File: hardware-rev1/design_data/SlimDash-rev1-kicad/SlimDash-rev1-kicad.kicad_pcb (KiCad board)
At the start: 2 copper layers, 157.1 x 131.5 mm, 140 parts, among them J1 AudioJack4, J2 AudioJack4, U1 TLV73333PDBV, U2 RP2040, U3 W25Q128JVS, Y1 Crystal_GND24

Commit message: update submodule
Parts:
- USB1: footprint ai03-2725_Type-C:HRO-TYPE-C-31-M-12-Assembly -> mzm_LCSC:USB-C_SMD-TYPE-C-31-M-12
- moved USB1 5.05 mm to (180.8, 43.5)
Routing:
- net Net-(LED31-DIN): track 0.00 -> 43.1 mm, vias 0 -> 4
- net Net-(LED33-DIN): track 0.00 -> 34.0 mm, vias 0 -> 5
- net Net-(LED34-DIN): track 0.00 -> 29.5 mm, vias 0 -> 2
- net Net-(LED32-DIN): track 4.70 -> 34.0 mm, vias 1 -> 3
- net Net-(LED30-DIN): track 0.00 -> 26.7 mm, vias 0 -> 2
- net Net-(JP1-B): track 7.71 -> 13.9 mm, vias 0 -> 1
- net GND: vias 89 -> 216

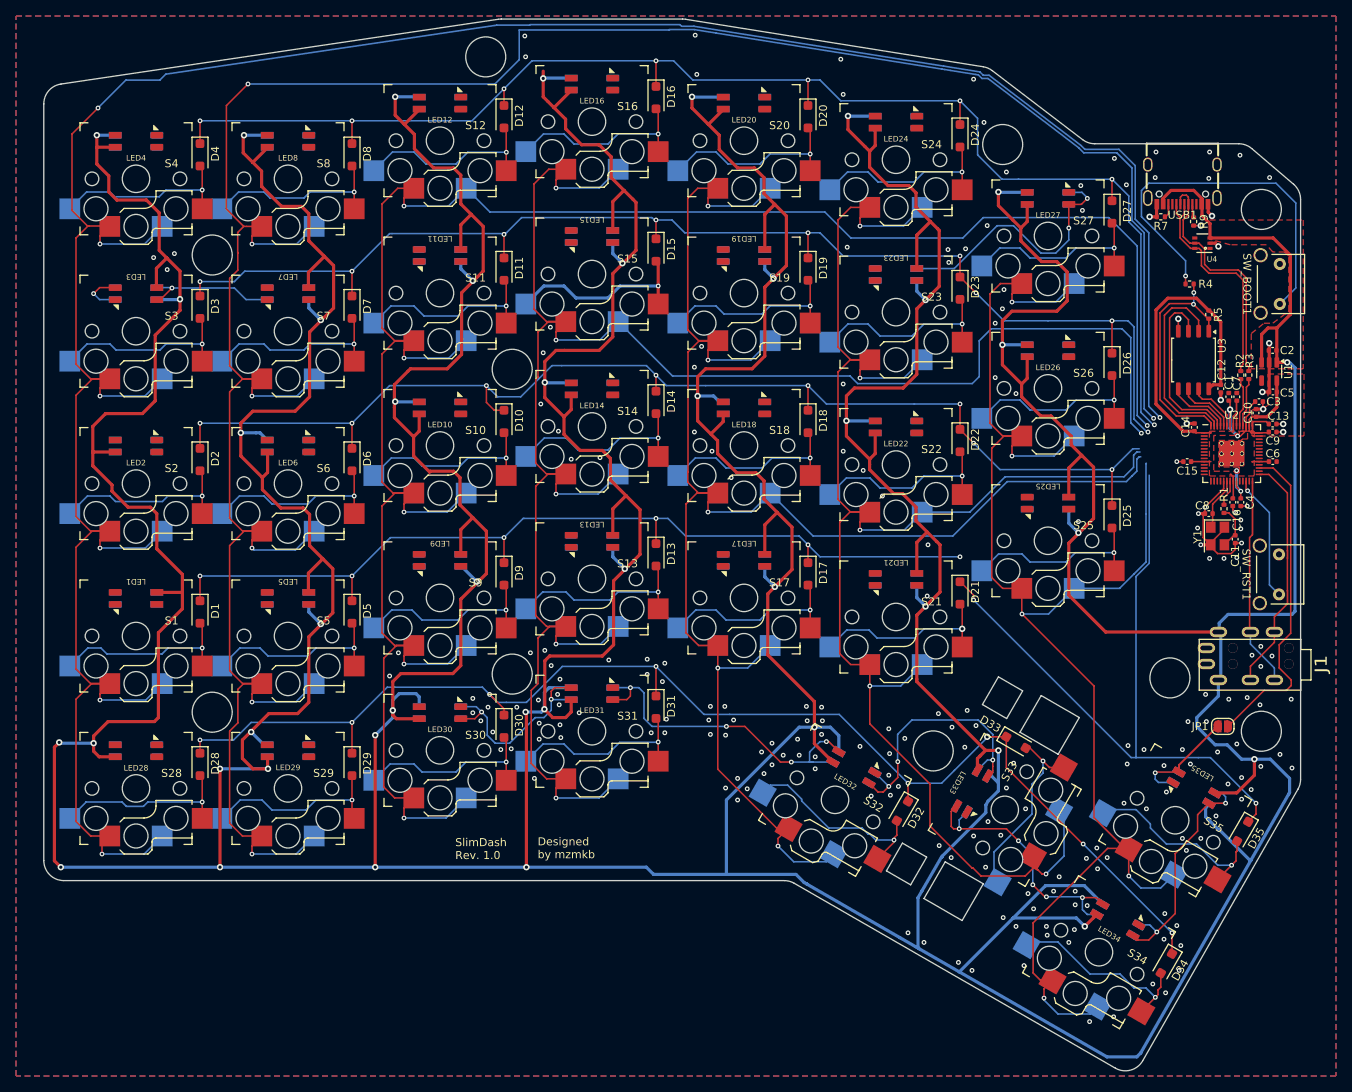
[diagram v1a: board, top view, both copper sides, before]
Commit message: wire updates on rgb leds
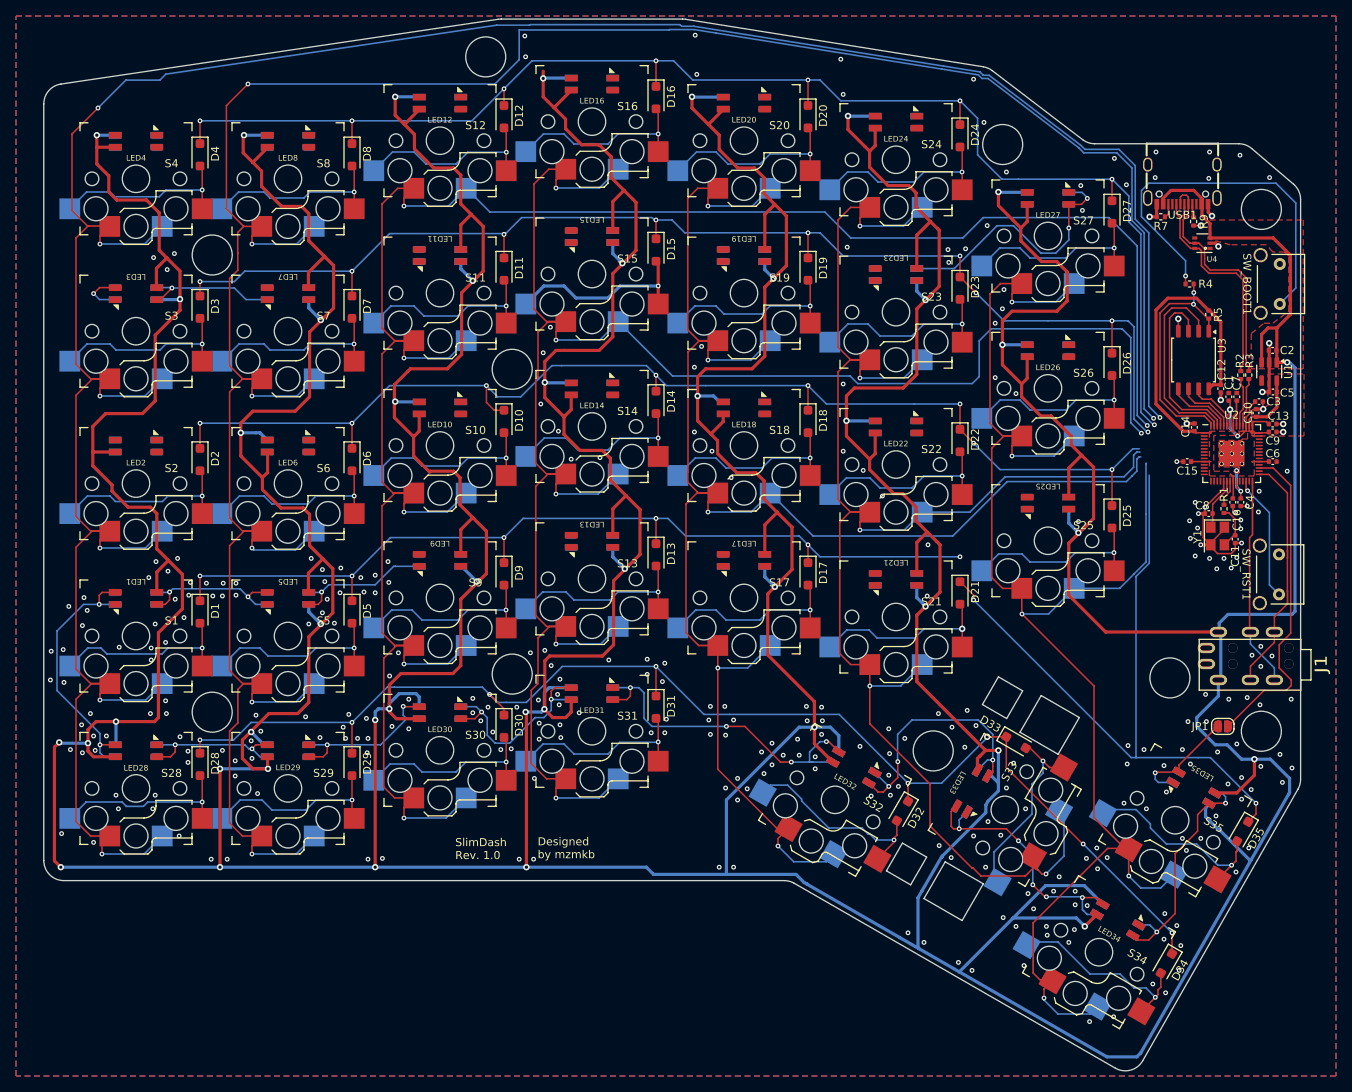
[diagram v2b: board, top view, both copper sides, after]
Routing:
- net Net-(LED1-DIN): track 0.00 -> 33.4 mm, vias 0 -> 2
- net Net-(LED29-DIN): track 0.00 -> 22.4 mm, vias 0 -> 2
- net Net-(LED1-DOUT): track 0.00 -> 20.2 mm, vias 0 -> 2
- net Net-(LED28-DIN): track 0.00 -> 20.0 mm, vias 0 -> 2
- net Net-(LED5-DOUT): track 0.00 -> 18.0 mm, vias 0 -> 1
- net +5V: track 1443.3 -> 1449.8 mm, vias 43 -> 44
- net GND: vias 216 -> 318

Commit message: finalize pcb layout
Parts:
- added C17: 10u, Capacitor_SMD:C_0402_1005Metric, F.Cu at (183.2, 98.0)
- added C18: 10u, Capacitor_SMD:C_0402_1005Metric, F.Cu at (187.1, 51.3)
- added TOOLING: JLCPCB_Tooling, mzm_misc:JLCPCB_Tooling, F.Cu at (42.2, 126.9)
- added TOOLING: JLCPCB_Tooling, mzm_misc:JLCPCB_Tooling, F.Cu at (172.3, 150.4)
- added TOOLING: JLCPCB_Tooling, mzm_misc:JLCPCB_Tooling, F.Cu at (42.0, 34.5)
- added U5: SN74LVC1T45DRL, mzm_LCSC:SOT-563_SN74LVC1T45DRLR, F.Cu at (182.4, 109.2)
- U4: value ~ -> SMF05CT1G
- moved JP1 0.47 mm to (185.7, 111.8), turned to -90 degrees
- moved C15 0.36 mm to (181.2, 78.5)
- turned LED1 to 0 degrees
- turned LED10 to 180 degrees
- turned LED11 to 0 degrees
- turned LED12 to 180 degrees
- turned LED13 to 0 degrees
- turned LED14 to 180 degrees
- turned LED15 to 0 degrees
- turned LED16 to 180 degrees
- turned LED17 to 0 degrees
- turned LED18 to 180 degrees
- turned LED19 to 0 degrees
- turned LED2 to 180 degrees
- turned LED20 to 180 degrees
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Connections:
- JP1 pad 1: DIN -> Net-(JP1-A)
- U2 pad 11: unconnected-(U2-GPIO8-Pad11) -> COL4
- U2 pad 12: unconnected-(U2-GPIO9-Pad12) -> COL6
- U2 pad 13: unconnected-(U2-GPIO10-Pad13) -> ROW4
- U2 pad 14: unconnected-(U2-GPIO11-Pad14) -> ROW3
- U2 pad 2: unconnected-(U2-GPIO0-Pad2) -> COL0
- U2 pad 3: unconnected-(U2-GPIO1-Pad3) -> COL1
- U2 pad 4: unconnected-(U2-GPIO2-Pad4) -> ROW0
- U2 pad 5: unconnected-(U2-GPIO3-Pad5) -> COL2
- U2 pad 6: unconnected-(U2-GPIO4-Pad6) -> ROW1
- U2 pad 7: unconnected-(U2-GPIO5-Pad7) -> COL3
- U2 pad 8: unconnected-(U2-GPIO6-Pad8) -> ROW2
- U2 pad 9: unconnected-(U2-GPIO7-Pad9) -> COL5
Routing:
- net ROW4: track 165.3 -> 214.1 mm, vias 8 -> 10
- net +3V3: track 68.9 -> 108.9 mm, vias 0 -> 2
- net Net-(LED25-DOUT): track 0.00 -> 32.4 mm, vias 0 -> 3
- net Net-(LED2-DOUT): track 6.12 -> 36.3 mm, vias 1 -> 2
- net Net-(LED24-DIN): track 0.00 -> 26.4 mm, vias 0 -> 2
- net Net-(LED22-DIN): track 0.00 -> 24.8 mm, vias 0 -> 2
- net Net-(LED21-DOUT): track 0.00 -> 24.3 mm, vias 0 -> 2
- net Net-(LED19-DOUT): track 0.00 -> 22.7 mm, vias 0 -> 2
- net Net-(LED18-DIN): track 0.00 -> 22.7 mm, vias 0 -> 2
- net Net-(LED15-DOUT): track 0.00 -> 22.4 mm, vias 0 -> 2
- net Net-(LED17-DOUT): track 0.00 -> 22.1 mm, vias 0 -> 2
- net Net-(LED13-DOUT): track 0.00 -> 22.0 mm, vias 0 -> 2
- net Net-(LED14-DIN): track 0.00 -> 21.5 mm, vias 0 -> 2
- net Net-(LED13-DIN): track 0.00 -> 21.3 mm, vias 0 -> 2
- net Net-(LED11-DIN): track 0.00 -> 21.1 mm, vias 0 -> 2
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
